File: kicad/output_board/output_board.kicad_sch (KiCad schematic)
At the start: 3 parts

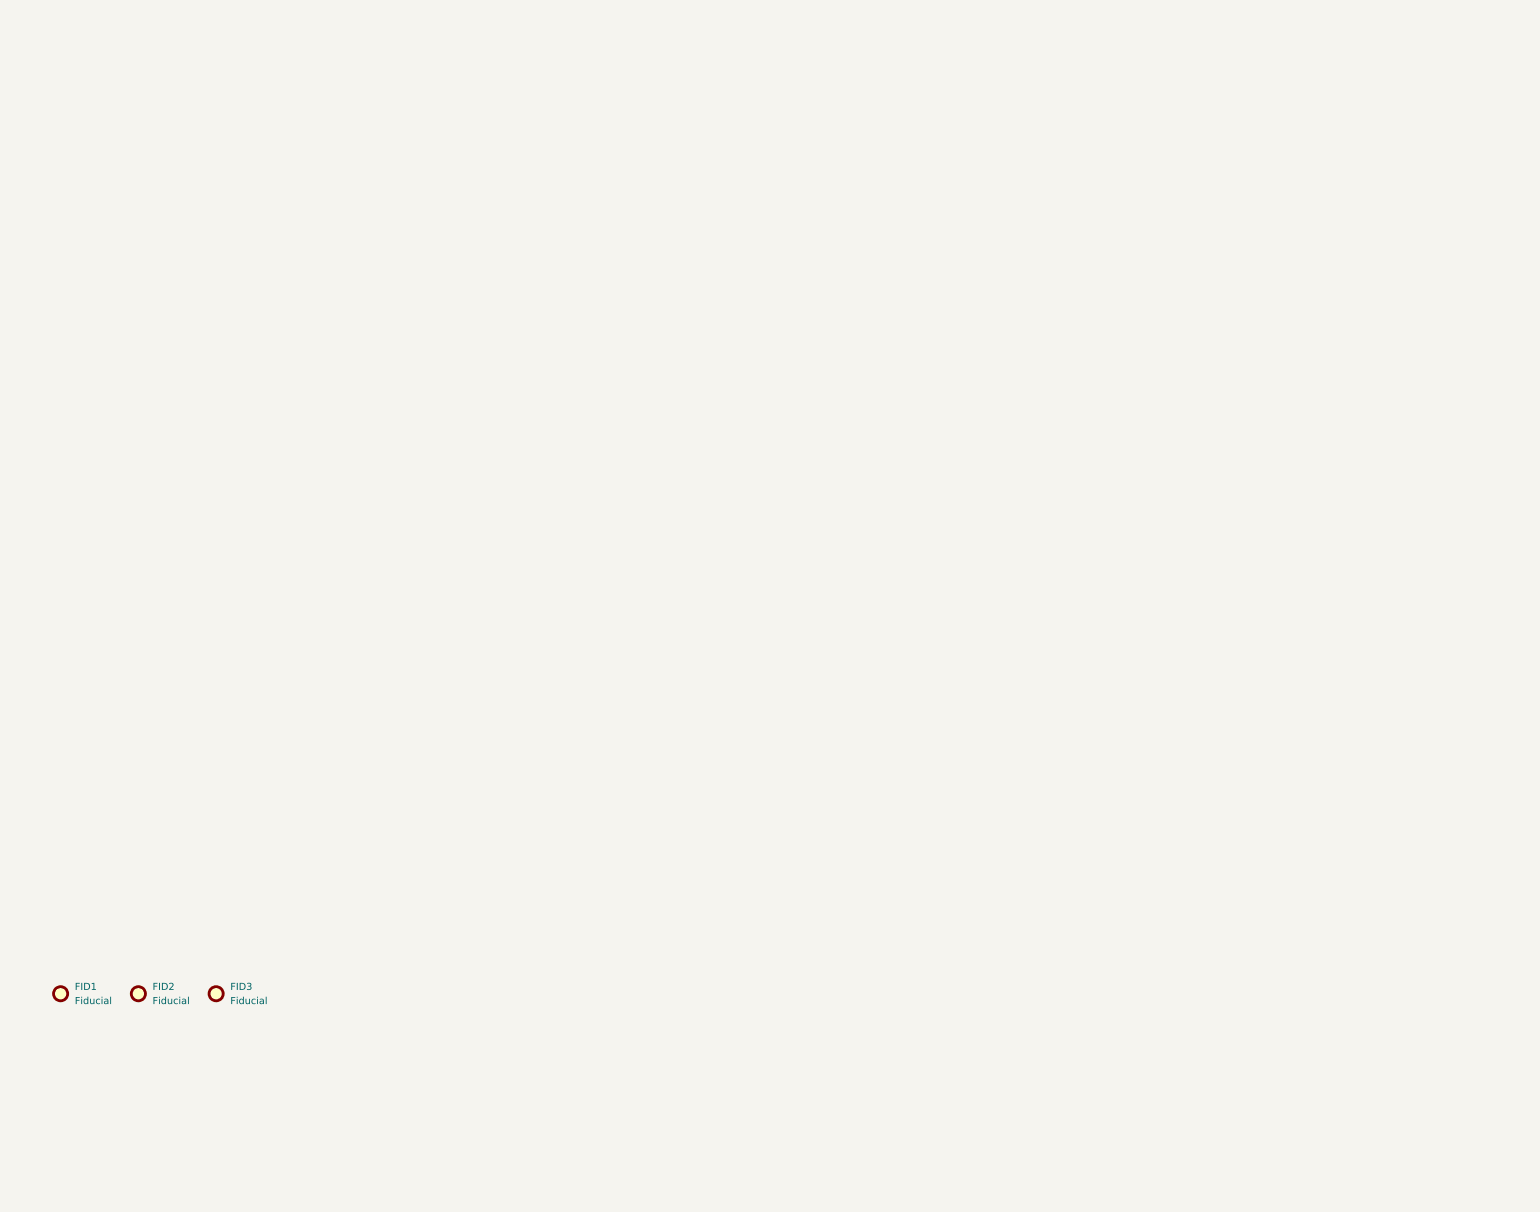
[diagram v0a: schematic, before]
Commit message: add output board
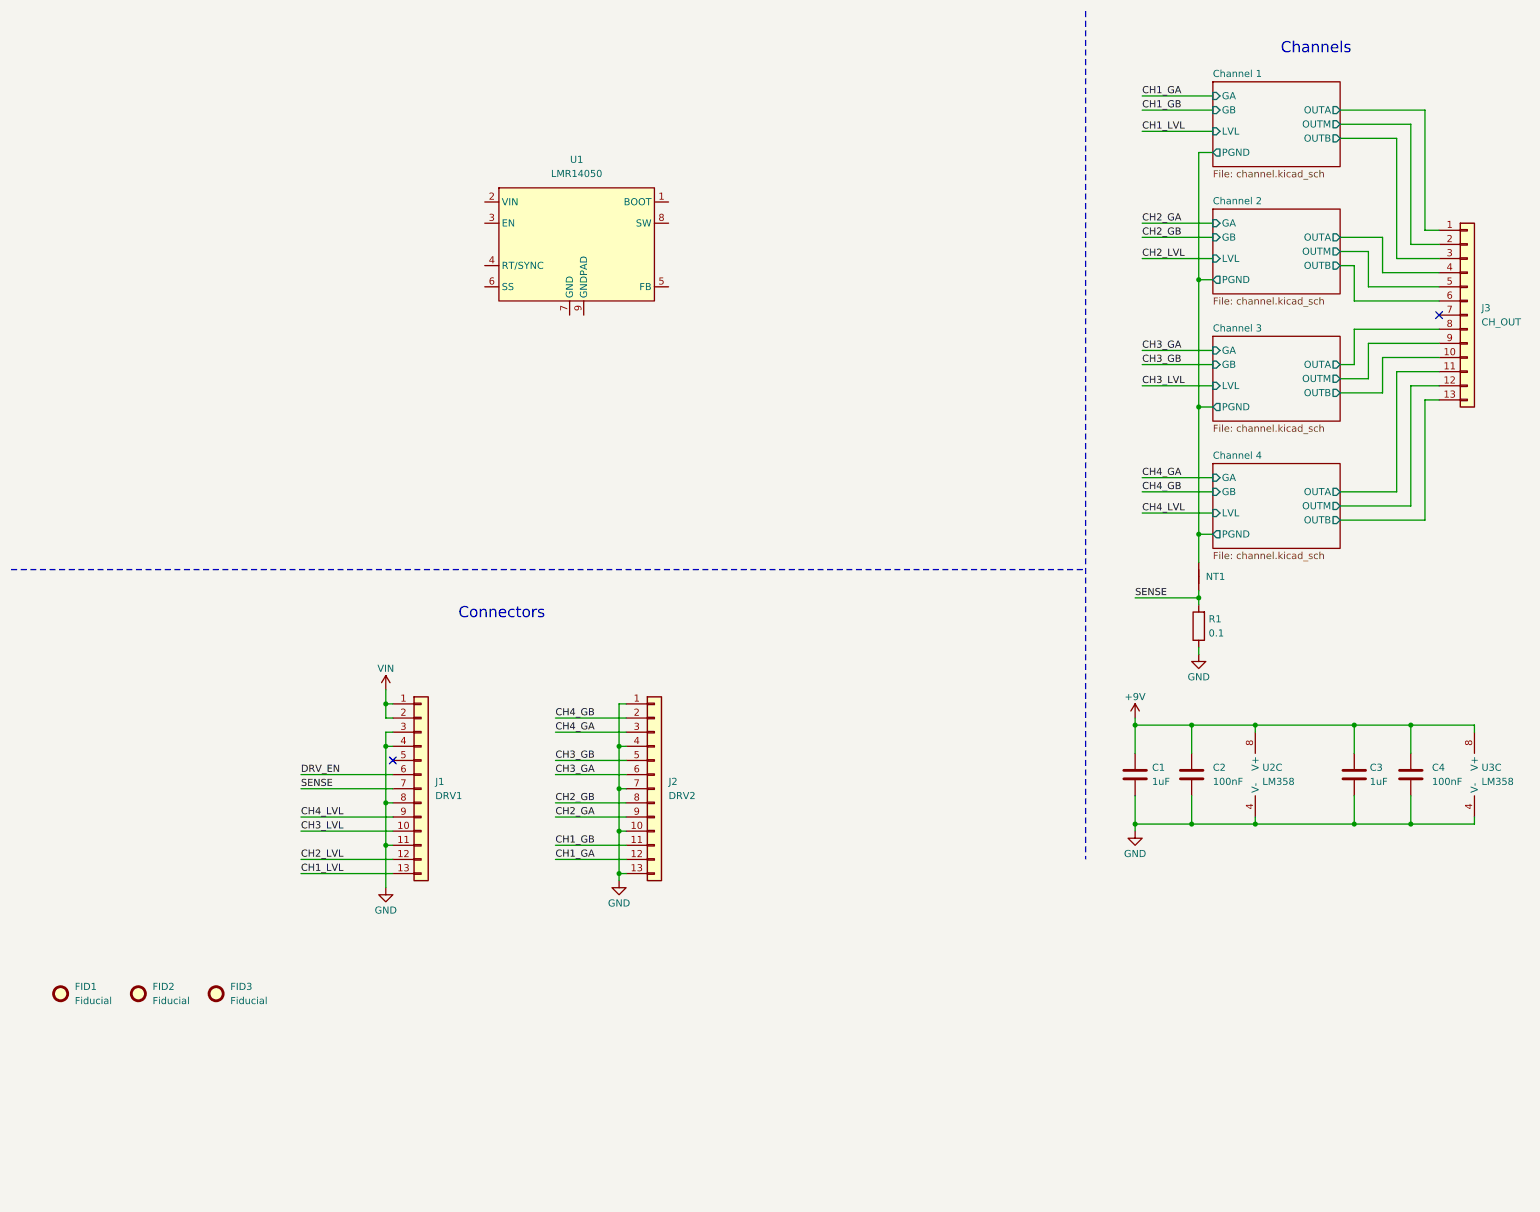
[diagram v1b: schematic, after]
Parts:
- added C1, C3: 1uF, Capacitor_SMD:C_0603_1608Metric, symbol Device:C
- added C2, C4: 100nF, Capacitor_SMD:C_0603_1608Metric, symbol Device:C
- added J1: DRV1, Connector_PinSocket_2.54mm:PinSocket_1x13_P2.54mm_Vertical, symbol Connector_Generic:Conn_01x13
- added J2: DRV2, Connector_PinSocket_2.54mm:PinSocket_1x13_P2.54mm_Vertical, symbol Connector_Generic:Conn_01x13
- added J3: CH_OUT, Connector_PinSocket_2.54mm:PinSocket_1x13_P2.54mm_Vertical, symbol Connector_Generic:Conn_01x13
- added NT1: ~, NetTie:NetTie-2_SMD_Pad2.0mm, symbol Device:NetTie_2
- added R1: 0.1, Resistor_SMD:R_1206_3216Metric, symbol Device:R
- added U1: LMR14050, symbol SaawLib:LMR14050
- added U2, U3: LM358, Package_SO:TSSOP-8_4.4x3mm_P0.65mm, symbol Device:Opamp_Dual
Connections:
- new net +9V: C1.1, C2.1, C3.1, C4.1, U2.8 (V+), U3.8 (V+)
- new net CH1_GA: J2.12 (Pin_12)
- new net CH1_GB: J2.11 (Pin_11)
- new net CH1_LVL: J1.13 (Pin_13)
- new net CH2_GA: J2.9 (Pin_9)
- new net CH2_GB: J2.8 (Pin_8)
- new net CH2_LVL: J1.12 (Pin_12)
- new net CH3_GA: J2.6 (Pin_6)
- new net CH3_GB: J2.5 (Pin_5)
- new net CH3_LVL: J1.10 (Pin_10)
- new net CH4_GA: J2.3 (Pin_3)
- new net CH4_GB: J2.2 (Pin_2)
- new net CH4_LVL: J1.9 (Pin_9)
- new net Channel 1/OUTA: J3.1 (Pin_1)
- new net Channel 1/OUTB: J3.3 (Pin_3)
- new net Channel 1/OUTM: J3.2 (Pin_2)
- new net Channel 1/PGND: NT1.2
- new net Channel 2/OUTA: J3.4 (Pin_4)
- new net Channel 2/OUTB: J3.6 (Pin_6)
- new net Channel 2/OUTM: J3.5 (Pin_5)
- new net Channel 3/OUTA: J3.8 (Pin_8)
- new net Channel 3/OUTB: J3.10 (Pin_10)
- new net Channel 3/OUTM: J3.9 (Pin_9)
- new net Channel 4/OUTA: J3.11 (Pin_11)
- new net Channel 4/OUTB: J3.13 (Pin_13)
- new net Channel 4/OUTM: J3.12 (Pin_12)
- new net DRV_EN: J1.6 (Pin_6)
- new net GND: C1.2, C2.2, C3.2, C4.2, J1.11 (Pin_11), J1.3 (Pin_3), J1.4 (Pin_4), J1.8 (Pin_8), J2.1 (Pin_1), J2.10 (Pin_10), J2.13 (Pin_13), J2.4 (Pin_4), J2.7 (Pin_7), R1.1, U2.4 (V-), U3.4 (V-)
- new net SENSE: J1.7 (Pin_7), NT1.1, R1.2
- new net VIN: J1.1 (Pin_1), J1.2 (Pin_2)
- no-connect marks 0 -> 2
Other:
- added sheet Channel 1 (channel.kicad_sch)
- added sheet Channel 2 (channel.kicad_sch)
- added sheet Channel 3 (channel.kicad_sch)
- added sheet Channel 4 (channel.kicad_sch)
- note added: "Channels"
- note added: "Connectors"

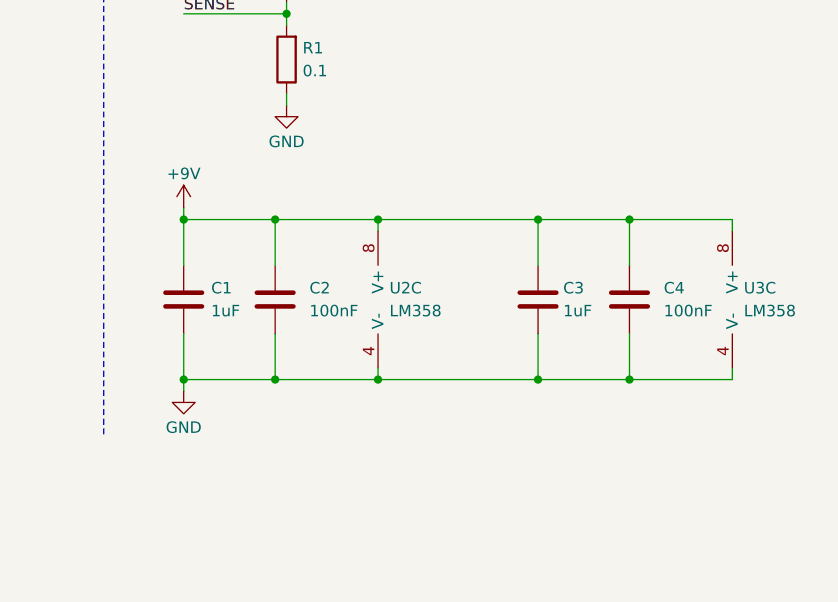
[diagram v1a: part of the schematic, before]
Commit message: update BOM prioritizing basic parts
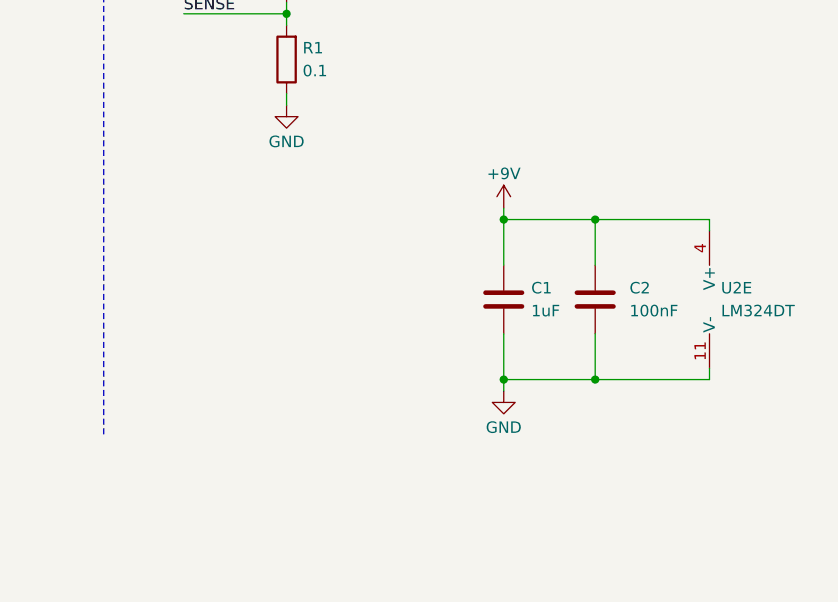
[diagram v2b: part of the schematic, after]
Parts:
- removed C3: 1uF, Capacitor_SMD:C_0603_1608Metric, symbol Device:C
- removed C4: 100nF, Capacitor_SMD:C_0603_1608Metric, symbol Device:C
- removed U2, U3: LM358, Package_SO:TSSOP-8_4.4x3mm_P0.65mm, symbol Device:Opamp_Dual
- added U2: LM324DT, Package_SO:SOIC-14_3.9x8.7mm_P1.27mm, symbol Amplifier_Operational:LM324
- C1: JLC (none) -> C15849; LCSC C5199872 -> (none); MOUSER 187-CL10B105KB8NQNC -> (none); MPN CL10B105KB8NQNC -> (none)
- C2: JLC (none) -> C14663; LCSC C1591 -> (none); MOUSER 187-CL10B104KB8NNNC -> (none); MPN CL10B104KB8NNNC -> (none)
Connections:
- net +9V: now also U2.4 (V+)
- net GND: now also U2.11 (V-)
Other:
- moved on the sheet: C1, C2

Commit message: add generation script
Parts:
- C1: JLC C15849 -> (none); LCSC (none) -> C15849; Service (none) -> PCBA
- C2: JLC C14663 -> (none); LCSC (none) -> C14663; Service (none) -> PCBA
- FID1, FID2, FID3, NT1: Service (none) -> PCBA;HandAssembly
- J1, J2, J3: Service (none) -> HandAssembly
- R1, U1: Service (none) -> PCBA
- U2: JLC C71035 -> (none); LCSC (none) -> C71035; Service (none) -> PCBA
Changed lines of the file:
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@@
 			)
 		)
-		(property "LCSC" ""
+		(property "LCSC" "C71035"
 			(at 275.59 149.86 0)
 			(effects
@@
 			)
 		)
-		(property "JLC" "C71035"
+		(property "Service" "PCBA"
 			(at 275.59 149.86 0)
 			(effects
@@
 			)
 		)
-		(property "JLC" ""
+		(property "Service" "PCBA;HandAssembly"
 			(at 35.56 189.23 0)
 			(effects
@@
 			)
 		)
-		(property "JLC" ""
+		(property "Service" "PCBA;HandAssembly"
 			(at 226.06 114.3 0)
 			(effects
@@
 			)
 		)
-		(property "LCSC" ""
+		(property "LCSC" "C14663"
 			(at 260.35 149.86 0)
 			(effects
@@
 			)
 		)
-		(property "JLC" "C14663"
+		(property "Service" "PCBA"
 			(at 260.35 149.86 0)
 			(effects
@@
 			)
 		)
-		(property "JLC" ""
+		(property "Service" "HandAssembly"
 			(at 128.27 152.4 0)
 			(effects
@@
 			)
 		)
-		(property "JLC" ""
+		(property "Service" "PCBA;HandAssembly"
 			(at 21.59 189.23 0)
 			(effects
@@
 			)
 		)
-		(property "LCSC" ""
+		(property "LCSC" "C15849"
 			(at 250.19 149.86 0)
 			(effects
@@
 			)
 		)
-		(property "JLC" "C15849"
+		(property "Service" "PCBA"
 			(at 250.19 149.86 0)
 			(effects
@@
 			)
 		)
-		(property "JLC" ""
+		(property "Service" "PCBA;HandAssembly"
 			(at 49.53 189.23 0)
 			(effects
@@
 			)
 		)
-		(property "JLC" ""
+		(property "Service" "HandAssembly"
 			(at 86.36 152.4 0)
 			(effects
@@
 			)
 		)
-		(property "JLC" ""
+		(property "Service" "PCBA"
 			(at 226.06 123.19 0)
 			(effects
@@
 			)
 		)
-		(property "JLC" ""
+		(property "Service" "HandAssembly"
 			(at 274.32 67.31 0)
 			(effects
@@
 			)
 		)
-		(property "JLC" ""
+		(property "Service" "PCBA"
 			(at 114.3 53.34 0)
 			(effects

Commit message: add psu
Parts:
- removed U1: LMR14050, symbol SaawLib:LMR14050
- added C1, C2: 10uF, Capacitor_SMD:C_0805_2012Metric, symbol Device:C
- added C3: 10nF, Capacitor_SMD:C_0603_1608Metric, symbol Device:C
- added C4: C_Polarized, symbol Device:C_Polarized
- added D1: D_Schottky, symbol Device:D_Schottky
- added L1: 15uH, ~, symbol Device:L_Ferrite
- added R1: 100k, Resistor_SMD:R_0603_1608Metric, symbol Device:R
- added R2: 10k, Resistor_SMD:R_0603_1608Metric, symbol Device:R
- added R3: 1.5k, Resistor_SMD:R_0603_1608Metric, symbol Device:R
- added TP1: 9V2, TestPoint:TestPoint_Pad_D1.0mm, symbol Connector:TestPoint_Small
- added U1: TPS5430DDA, Package_SO:TI_SO-PowerPAD-8_ThermalVias, symbol Regulator_Switching:TPS5430DDA
- renumbered C1 to C5, C2 to C6, R1 to R4
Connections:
- net +9V: now also C4.1, L1.2, R2.2, TP1.1
- net DRV_EN: now also R1.1, U1.5 (EN)
- net GND: now also C1.1, C2.1, C4.2, D1.2 (A), R1.2, R3.2, U1.6 (GND), U1.9 (GNDPAD)
- net VIN: now also C1.2, C2.2, U1.7 (VIN)
- new net: R2.1, R3.1, U1.4 (VSENSE)
- new net: C3.2, D1.1 (K), L1.1, U1.8 (PH)
- new net: C3.1, U1.1 (BOOT)
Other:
- note added: "3A max (4A peak)"
- note added: "9V Reg"

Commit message: update bom
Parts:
- C4: value C_Polarized -> ?; Service PCBA -> (none)
- D1: value D_Schottky -> SS34; footprint (none) -> Diode_SMD:D_SMA; LCSC (none) -> C8678
- J1, J2, J3: LCSC (none) -> C2897376
- R3: LCSC (none) -> C22843
- R4: footprint Resistor_SMD:R_1206_3216Metric -> Resistor_SMD:R_2512_6332Metric; LCSC (none) -> C165698
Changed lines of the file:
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@@
 			)
 		)
-		(property "Datasheet" "~"
+		(property "Datasheet" "https://www.lcsc.com/datasheet/lcsc_datasheet_2206010130_UNI-ROYAL-Uniroyal-Elec-0603WAF1501T5E_C22843.pdf"
 			(at 165.1 80.01 0)
 			(effects
@@
 		)
 		(property "Service" "PCBA"
+			(at 165.1 80.01 0)
+			(effects
+				(font
+					(size 1.27 1.27)
+				)
+				(hide yes)
+			)
+		)
+		(property "LCSC" "C22843"
 			(at 165.1 80.01 0)
 			(effects
@@
 			)
 		)
-		(property "Datasheet" "~"
+		(property "Datasheet" "https://www.lcsc.com/datasheet/lcsc_datasheet_2306091006_HCTL-PM254-1-13-Z-8-5_C2897376.pdf"
 			(at 128.27 152.4 0)
 			(effects
@@
 			)
 		)
-		(property "LCSC" ""
+		(property "LCSC" "C2897376"
 			(at 128.27 152.4 0)
 			(effects
@@
 			)
 		)
-		(property "Datasheet" "~"
+		(property "Datasheet" "https://www.lcsc.com/datasheet/lcsc_datasheet_2404260921_cjiang--Changjiang-Microelectronics-Tech-FXL0630-150-M_C177243.pdf"
 			(at 132.08 57.15 0)
 			(effects
@@
 			)
 		)
-		(property "Value" "D_Schottky"
+		(property "Value" "SS34"
 			(at 124.46 63.1824 90)
 			(effects
@@
 			)
 		)
-		(property "Footprint" ""
+		(property "Footprint" "Diode_SMD:D_SMA"
 			(at 121.92 62.23 0)
 			(effects
@@
 			)
 		)
-		(property "Datasheet" "~"
+		(property "Datasheet" "https://www.lcsc.com/datasheet/lcsc_datasheet_2303141100_MDD-Microdiode-Electronics-SS34_C8678.pdf"
 			(at 121.92 62.23 0)
 			(effects
@@
 		)
 		(property "Service" "PCBA"
+			(at 121.92 62.23 0)
+			(effects
+				(font
+					(size 1.27 1.27)
+				)
+				(hide yes)
+			)
+		)
+		(property "LCSC" "C8678"
 			(at 121.92 62.23 0)
 			(effects
@@
 			)
 		)
-		(property "Datasheet" "~"
+		(property "Datasheet" "https://www.lcsc.com/datasheet/lcsc_datasheet_2306091006_HCTL-PM254-1-13-Z-8-5_C2897376.pdf"
 			(at 86.36 152.4 0)
 			(effects
@@
 			)
 		)
-		(property "LCSC" ""
+		(property "LCSC" "C2897376"
 			(at 86.36 152.4 0)
 			(effects
@@
 			)
 		)
-		(property "Value" "C_Polarized"
+		(property "Value" "?"
 			(at 146.05 62.6109 0)
 			(effects
@@
 			)
 		)
-		(property "Service" "PCBA"
+		(property "Service" ""
 			(at 142.24 62.23 0)
 			(effects
@@
 			)
 		)
-		(property "Footprint" "Resistor_SMD:R_1206_3216Metric"
+		(property "Footprint" "Resistor_SMD:R_2512_6332Metric"
 			(at 227.838 123.19 90)
 			(effects
@@
 			)
 		)
-		(property "Datasheet" "~"
+		(property "Datasheet" "https://www.lcsc.com/datasheet/lcsc_datasheet_1810271822_YAGEO-PE2512FKE7W0R1L_C165698.pdf"
 			(at 226.06 123.19 0)
 			(effects
@@
 		)
 		(property "Service" "PCBA"
+			(at 226.06 123.19 0)
+			(effects
+				(font
+					(size 1.27 1.27)
+				)
+				(hide yes)
+			)
+		)
+		(property "LCSC" "C165698"
 			(at 226.06 123.19 0)
 			(effects
@@
 			)
 		)
-		(property "Datasheet" "~"
+		(property "Datasheet" "https://www.lcsc.com/datasheet/lcsc_datasheet_2306091006_HCTL-PM254-1-13-Z-8-5_C2897376.pdf"
 			(at 274.32 67.31 0)
 			(effects
@@
 			)
 		)
-		(property "LCSC" ""
+		(property "LCSC" "C2897376"
 			(at 274.32 67.31 0)
 			(effects
